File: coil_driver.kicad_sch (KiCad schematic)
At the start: 23 parts, among them J6 Conn_01x02, Q3 Si7465DP, Q4 CSD18563Q5A, U10 TC4426xOA, U15 MCP9808T-E/MS, U8 INA180A2, U9 LM393DR

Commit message: footprints
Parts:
- C18: footprint (none) -> Capacitor_SMD:C_0402_1005Metric
- C_INA1: renamed from C_INA; footprint (none) -> Capacitor_SMD:C_0402_1005Metric
- C_MCP1: renamed from C_MCP; footprint (none) -> Capacitor_SMD:C_0402_1005Metric
- C_TC1: renamed from C_TC; footprint (none) -> Capacitor_SMD:C_0402_1005Metric
- J6: footprint (none) -> Connector_Wire:SolderWire-2.5sqmm_1x02_P8.8mm_D2.4mm_OD4.4mm
- NT1: footprint (none) -> NetTie:NetTie-2_SMD_Pad0.5mm
- R10, R6, R7, R8, R_GS_Q3: footprint (none) -> Resistor_SMD:R_0402_1005Metric
- R21, R9: footprint (none) -> Resistor_SMD:R_0603_1608Metric
- R_G3_HS1: renamed from R_G3_HS; footprint (none) -> Resistor_SMD:R_0402_1005Metric
- R_SHUNT1: renamed from R_SHUNT; footprint (none) -> Resistor_SMD:R_2512_6332Metric
- U15: footprint MSOP8_MC_MCH -> Package_SO:MSOP-8_3x3mm_P0.65mm
- U9: footprint D8 -> Package_SO:SOIC-8_3.9x4.9mm_P1.27mm
- renumbered D_FLY to D_FLY1
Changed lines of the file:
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@@
 			)
 		)
-		(property "Footprint" "D8"
+		(property "Footprint" "Package_SO:SOIC-8_3.9x4.9mm_P1.27mm"
 			(at 118.11 72.39 0)
 			(effects
@@
 			)
 		)
-		(property "Footprint" ""
+		(property "Footprint" "Resistor_SMD:R_0402_1005Metric"
 			(at 38.862 81.28 90)
 			(effects
@@
 			)
 		)
-		(property "Footprint" ""
+		(property "Footprint" "NetTie:NetTie-2_SMD_Pad0.5mm"
 			(at 62.23 99.06 0)
 			(effects
@@
 			)
 		)
-		(property "Footprint" ""
+		(property "Footprint" "Resistor_SMD:R_0402_1005Metric"
 			(at 109.982 67.31 90)
 			(effects
@@
 			)
 		)
-		(property "Footprint" ""
+		(property "Footprint" "Connector_Wire:SolderWire-2.5sqmm_1x02_P8.8mm_D2.4mm_OD4.4mm"
 			(at 80.01 55.88 0)
 			(effects
@@
 			)
 		)
-		(property "Footprint" ""
+		(property "Footprint" "Resistor_SMD:R_0402_1005Metric"
 			(at 120.142 39.37 90)
 			(effects
@@
 			)
 		)
-		(property "Footprint" ""
+		(property "Footprint" "Capacitor_SMD:C_0402_1005Metric"
 			(at 122.8852 53.34 0)
 			(effects
@@
 		(dnp no)
 		(fields_autoplaced yes)
-		(property "Reference" "C_INA"
+		(property "Reference" "C_INA1"
 			(at 129.54 24.1299 0)
 			(effects
@@
 			)
 		)
-		(property "Footprint" ""
+		(property "Footprint" "Capacitor_SMD:C_0402_1005Metric"
 			(at 126.6952 29.21 0)
 			(effects
@@
 			(project ""
 				(path "/96bcf3cc-a3b8-4386-8709-07acaf7b6253/553700f1-75c4-49dd-b240-b79fee22db17"
-					(reference "C_INA")
+					(reference "C_INA1")
 					(unit 1)
 				)
@@
 		(dnp no)
 		(fields_autoplaced yes)
-		(property "Reference" "D_FLY"
+		(property "Reference" "D_FLY1"
 			(at 84.7725 40.64 0)
 			(effects
@@
 			(project ""
 				(path "/96bcf3cc-a3b8-4386-8709-07acaf7b6253/553700f1-75c4-49dd-b240-b79fee22db17"
-					(reference "D_FLY")
+					(reference "D_FLY1")
 					(unit 1)
 				)
@@
 		(dnp no)
 		(fields_autoplaced yes)
-		(property "Reference" "C_MCP"
+		(property "Reference" "C_MCP1"
 			(at 157.48 100.3299 0)
 			(effects
@@
 			)
 		)
-		(property "Footprint" ""
+		(property "Footprint" "Capacitor_SMD:C_0402_1005Metric"
 			(at 154.6352 105.41 0)
 			(effects
@@
 			(project ""
 				(path "/96bcf3cc-a3b8-4386-8709-07acaf7b6253/553700f1-75c4-49dd-b240-b79fee22db17"
-					(reference "C_MCP")
+					(reference "C_MCP1")
 					(unit 1)
 				)
@@
 			)
 		)
-		(property "Footprint" "MSOP8_MC_MCH"
+		(property "Footprint" "Package_SO:MSOP-8_3x3mm_P0.65mm"
 			(at 72.39 97.79 0)
 			(effects
@@
 		(dnp no)
 		(fields_autoplaced yes)
-		(property "Reference" "R_G3_HS"
+		(property "Reference" "R_G3_HS1"
 			(at 110.49 134.6199 0)
 			(effects
@@
 			)
 		)
-		(property "Footprint" ""
+		(property "Footprint" "Resistor_SMD:R_0402_1005Metric"
 			(at 106.172 135.89 90)
 			(effects
@@
 			(project ""
 				(path "/96bcf3cc-a3b8-4386-8709-07acaf7b6253/553700f1-75c4-49dd-b240-b79fee22db17"
-					(reference "R_G3_HS")
+					(reference "R_G3_HS1")
 					(unit 1)
 				)
@@
 			)
 		)
-		(property "Footprint" ""
+		(property "Footprint" "Resistor_SMD:R_0402_1005Metric"
 			(at 146.812 44.45 90)
 			(effects
@@
 			)
 		)
-		(property "Footprint" ""
+		(property "Footprint" "Resistor_SMD:R_0402_1005Metric"
 			(at 146.812 53.34 90)
 			(effects
@@
 		(dnp no)
 		(fields_autoplaced yes)
-		(property "Reference" "C_TC"
+		(property "Reference" "C_TC1"
 			(at 105.41 120.6499 0)
 			(effects
@@
 			)
 		)
-		(property "Footprint" ""
+		(property "Footprint" "Capacitor_SMD:C_0402_1005Metric"
 			(at 102.5652 125.73 0)
 			(effects
@@
 			(project ""
 				(path "/96bcf3cc-a3b8-4386-8709-07acaf7b6253/553700f1-75c4-49dd-b240-b79fee22db17"
-					(reference "C_TC")
+					(reference "C_TC1")
 					(unit 1)
 				)
@@
 			)
 		)
-		(property "Footprint" ""
+		(property "Footprint" "Resistor_SMD:R_0603_1608Metric"
 			(at 117.602 67.31 90)
 			(effects
@@
 			)
 		)
-		(property "Footprint" ""
+		(property "Footprint" "Resistor_SMD:R_0603_1608Metric"
 			(at 71.882 62.23 90)
 			(effects
@@
 		(dnp no)
 		(fields_autoplaced yes)
-		(property "Reference" "R_SHUNT"
+		(property "Reference" "R_SHUNT1"
 			(at 57.15 55.8799 0)
 			(effects
@@
 			)
 		)
-		(property "Footprint" ""
+		(property "Footprint" "Resistor_SMD:R_2512_6332Metric"
 			(at 52.832 57.15 90)
 			(effects
@@
 			(project ""
 				(path "/96bcf3cc-a3b8-4386-8709-07acaf7b6253/553700f1-75c4-49dd-b240-b79fee22db17"
-					(reference "R_SHUNT")
-					(unit 1)
-				)
+					(reference "R_SHUNT1")
+					(unit 1)
+				)

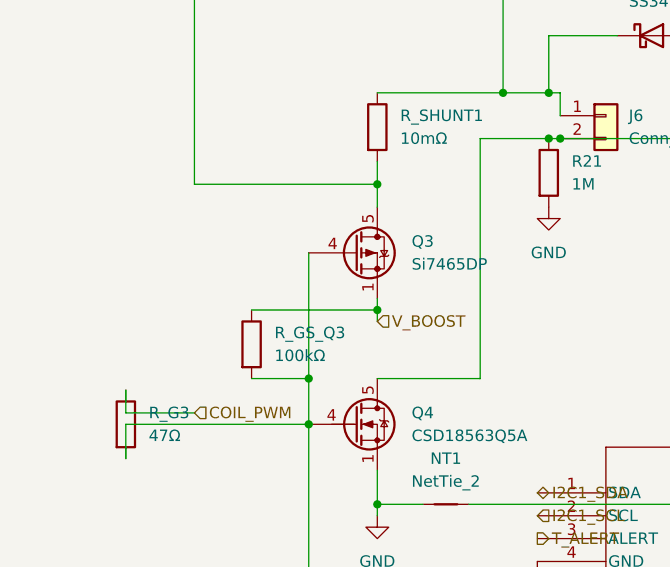
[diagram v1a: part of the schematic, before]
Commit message: fix missing connections, complete footprints
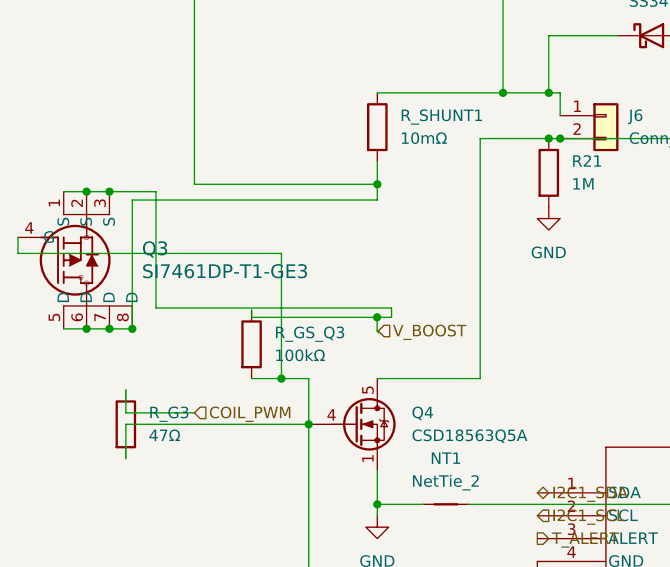
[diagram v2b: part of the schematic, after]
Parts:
- removed Q3: Si7465DP, Package_SO:PowerPAK_SO-8_Single, symbol Si7461DP:Si7465DP
- added Q3: SI7461DP-T1-GE3, Package_SO:PowerPAK_SO-8_Single, symbol Si7461DP-T1-GE3:SI7461DP-T1-GE3
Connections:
- net V_BOOST: now also Q3.1 (S), Q3.2 (S), Q3.3 (S)
- net at Q4.4 (G), R_G3.2, R_G3_HS1.2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: now also Q3.4 (G)
- net at R_SHUNT1.2, U8.3 (+): now also Q3.5 (D), Q3.6 (D), Q3.7 (D), Q3.8 (D)

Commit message: net labels
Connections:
- net Q4_GATE: now reaches Q3.4 (G), Q4.4 (G), R_G3.2, R_G3_HS1.2, R_GS_Q3.2
- net COIL-: now reaches D_FLY1.2 (A), J6.2 (Pin_2), Q4.5 (D), R21.1
- net COMP_IN-: now reaches R7.2, R8.1, U9.2 (1IN-)
- net OC_THRESH+: now reaches C18.1, R6.2, R9.1, U9.3 (1IN+)
- net SHUNT_LO: now reaches NT1.2, U8.2 (GND), U9.4 (GND)
- net DRIVER_OUT: now reaches R_G3_HS1.1, U10.7 (~{OUT_A})
- net COIL+: now reaches D_FLY1.1 (K), J6.1 (Pin_1), R_SHUNT1.1, U8.4 (-)
- net OPAMP_IN+: now reaches Q3.5 (D), Q3.6 (D), Q3.7 (D), Q3.8 (D), R_SHUNT1.2, U8.3 (+)
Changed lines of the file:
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@@
+	(wire
+		(pts
+			(xy 87.5518 144.78) (xy 86.36 144.78)
+		)
+		(stroke
+			(width 0)
+			(type default)
+		)
+	)
 	(wire
 		(pts
@@
 	(wire
 		(pts
+			(xy 87.5518 147.9984) (xy 87.5518 144.78)
+		)
+		(stroke
+			(width 0)
+			(type default)
+		)
+	)
+	(wire
+		(pts
 			(xy 118.11 86.36) (xy 106.68 86.36)
 		)
@@
 	(wire
 		(pts
+			(xy 86.1936 147.9984) (xy 87.5518 147.9984)
+		)
+		(stroke
+			(width 0)
+			(type default)
+		)
+	)
+	(wire
+		(pts
 			(xy 43.9574 85.09) (xy 46.99 85.09)
 		)
@@
 			(width 0)
 			(type default)
+		)
+	)
+	(label "SHUNT_LO"
+		(at 67.3104 99.06 0)
+		(effects
+			(font
+				(size 1.27 1.27)
+			)
+			(justify left bottom)
+		)
+	)
+	(label "OC_THRESH+"
+		(at 114.3 75.305 0)
+		(effects
+			(font
+				(size 1.27 1.27)
+			)
+			(justify left bottom)
+		)
+	)
+	(label "COIL-"
+		(at 88.9 52.8305 0)
+		(effects
+			(font
+				(size 1.27 1.27)
+			)
+			(justify left bottom)
+		)
+	)
+	(label "OPAMP_IN+"
+		(at 83.5102 33.02 0)
+		(effects
+			(font
+				(size 1.27 1.27)
+			)
+			(justify left bottom)
+		)
+	)
+	(label "DRIVER_OUT"
+		(at 104.5741 132.08 0)
+		(effects
+			(font
+				(size 1.27 1.27)
+			)
+			(justify left bottom)
+		)
+	)
+	(label "COMP_IN-"
+		(at 129.54 57.704 0)
+		(effects
+			(font
+				(size 1.27 1.27)
+			)
+			(justify left bottom)
+		)
+	)
+	(label "COIL+"
+		(at 85.894 38.1 0)
+		(effects
+			(font
+				(size 1.27 1.27)
+			)
+			(justify left bottom)
+		)
+	)
+	(label "OPAMP_REF"
+		(at 87.5518 146.3209 0)
+		(effects
+			(font
+				(size 1.27 1.27)
+			)
+			(justify left bottom)
+		)
+	)
+	(label "Q4_GATE"
+		(at 37.2982 71.1811 0)
+		(effects
+			(font
+				(size 1.27 1.27)
+			)
+			(justify left bottom)
 		)
 	)
@@
 	(symbol
 		(lib_id "power:GND")
-		(at 86.36 144.78 0)
+		(at 86.1936 147.9984 0)
 		(unit 1)
 		(exclude_from_sim no)
@@
 		(fields_autoplaced yes)
 		(property "Reference" "#PWR045"
-			(at 86.36 151.13 0)
+			(at 86.1936 154.3484 0)
 			(effects
 				(font
@@
 		)
 		(property "Value" "GND"
-			(at 86.36 149.86 0)
+			(at 86.1936 153.0784 0)
 			(effects
 				(font
@@
 		)
 		(property "Footprint" ""
-			(at 86.36 144.78 0)
+			(at 86.1936 147.9984 0)
 			(effects
 				(font
@@
 		)
 		(property "Datasheet" ""
-			(at 86.36 144.78 0)
+			(at 86.1936 147.9984 0)
 			(effects
 				(font
@@
 		)
 		(property "Description" "Power symbol creates a global label with name \"GND\" , ground"
-			(at 86.36 144.78 0)
-			(effects
-				(font
+			(at 86.1936 147.9984 0)
+			(effects
+				(font

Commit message: fixed labels
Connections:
- net SHUNT_LO renamed AGND
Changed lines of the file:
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@@
-	(wire
-		(pts
-			(xy 87.5518 144.78) (xy 86.36 144.78)
-		)
-		(stroke
-			(width 0)
-			(type default)
-		)
-	)
 	(wire
 		(pts
@@
 	(wire
 		(pts
+			(xy 86.1936 147.9984) (xy 86.1936 144.78)
+		)
+		(stroke
+			(width 0)
+			(type default)
+		)
+	)
+	(wire
+		(pts
 			(xy 54.61 60.96) (xy 54.61 63.5)
 		)
@@
 	(wire
 		(pts
-			(xy 87.5518 147.9984) (xy 87.5518 144.78)
-		)
-		(stroke
-			(width 0)
-			(type default)
-		)
-	)
-	(wire
-		(pts
 			(xy 118.11 86.36) (xy 106.68 86.36)
 		)
@@
 	(wire
 		(pts
+			(xy 86.1936 144.78) (xy 86.36 144.78)
+		)
+		(stroke
+			(width 0)
+			(type default)
+		)
+	)
+	(wire
+		(pts
 			(xy 34.29 33.02) (xy 101.6 33.02)
 		)
@@
 	(wire
 		(pts
-			(xy 86.1936 147.9984) (xy 87.5518 147.9984)
-		)
-		(stroke
-			(width 0)
-			(type default)
-		)
-	)
-	(wire
-		(pts
 			(xy 43.9574 85.09) (xy 46.99 85.09)
 		)
@@
 			(width 0)
 			(type default)
-		)
-	)
-	(label "SHUNT_LO"
-		(at 67.3104 99.06 0)
-		(effects
-			(font
-				(size 1.27 1.27)
-			)
-			(justify left bottom)
 		)
 	)
@@
 		)
 	)
+	(label "AGND"
+		(at 106.68 48.6788 0)
+		(effects
+			(font
+				(size 1.27 1.27)
+			)
+			(justify left bottom)
+		)
+	)
 	(label "DRIVER_OUT"
 		(at 104.5741 132.08 0)
@@
 		(effects
 			(font
-				(size 1.27 1.27)
-			)
-			(justify left bottom)
-		)
-	)
-	(label "OPAMP_REF"
-		(at 87.5518 146.3209 0)
-		(effects
-			(font

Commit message: add missing footprints
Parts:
- R_G3: footprint (none) -> Resistor_SMD:R_0402_1005Metric
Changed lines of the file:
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@@
 			)
 		)
-		(property "Footprint" ""
+		(property "Footprint" "Resistor_SMD:R_0402_1005Metric"
 			(at 24.892 90.17 90)
 			(effects
